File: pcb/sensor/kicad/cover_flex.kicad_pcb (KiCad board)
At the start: 2 copper layers, 32 x 38.7 mm, 7 parts, among them J1 S7081-42R +5V, J2 S7081-42R GND, J3 S7081-42R VBAT, J4 S7081-42R GND, U1 TLV75533PDBVR

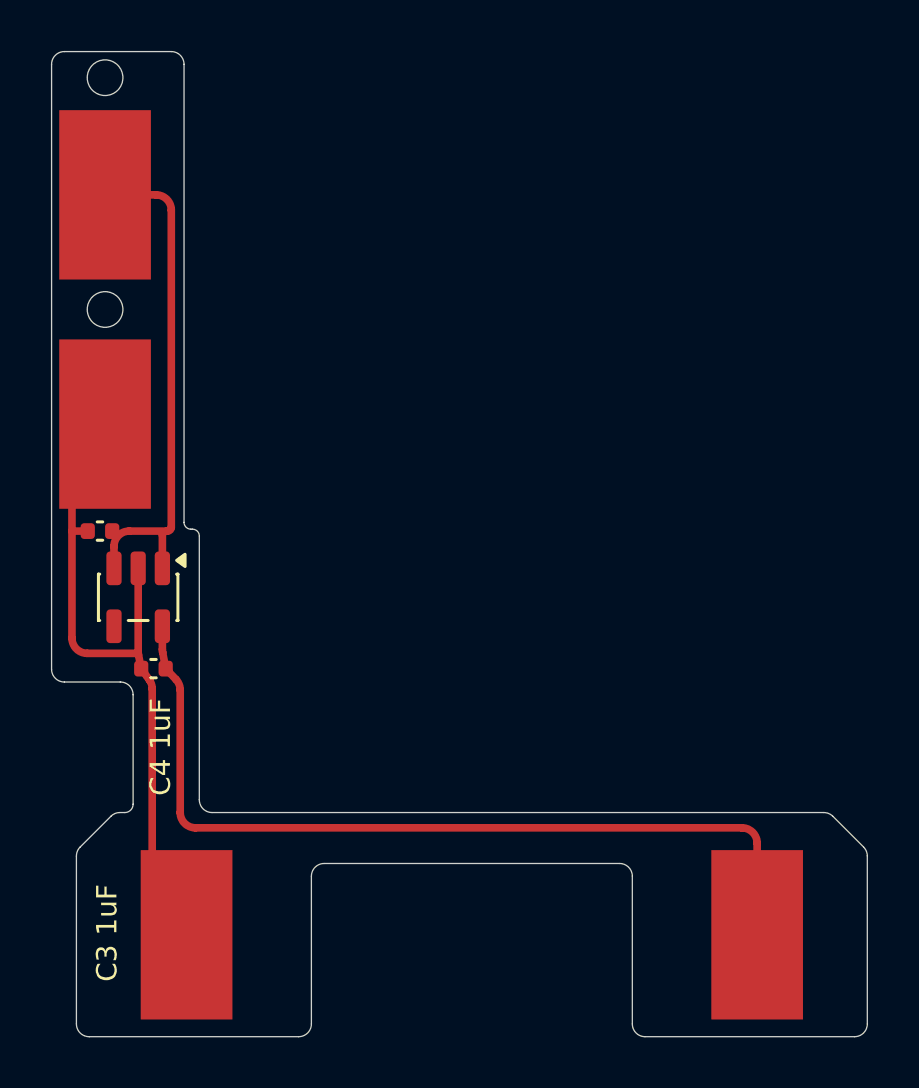
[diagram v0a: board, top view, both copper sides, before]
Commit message: Back cover: snap hooks for the flex, stronger magnet clips, rounded contact posts; #6 countersink and PLATE_Y on the trim
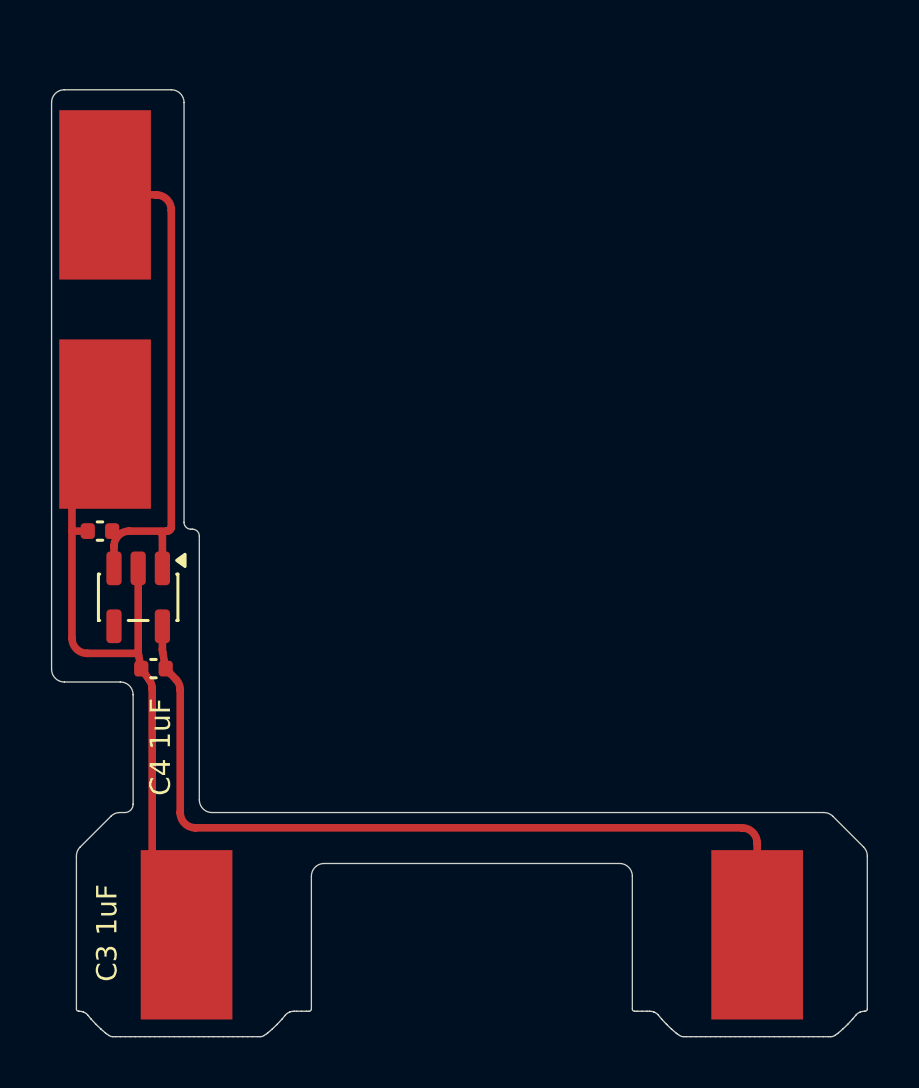
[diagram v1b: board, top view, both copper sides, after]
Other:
- board size 32 x 38.7 mm -> 32 x 37.2 mm
- board text added: "STIFFENER FR4 0.8 mm, back side, flush with the long edges (snap hooks)"
- board text removed: "STIFFENER FR4 0.3 mm, back side, with the peg holes"

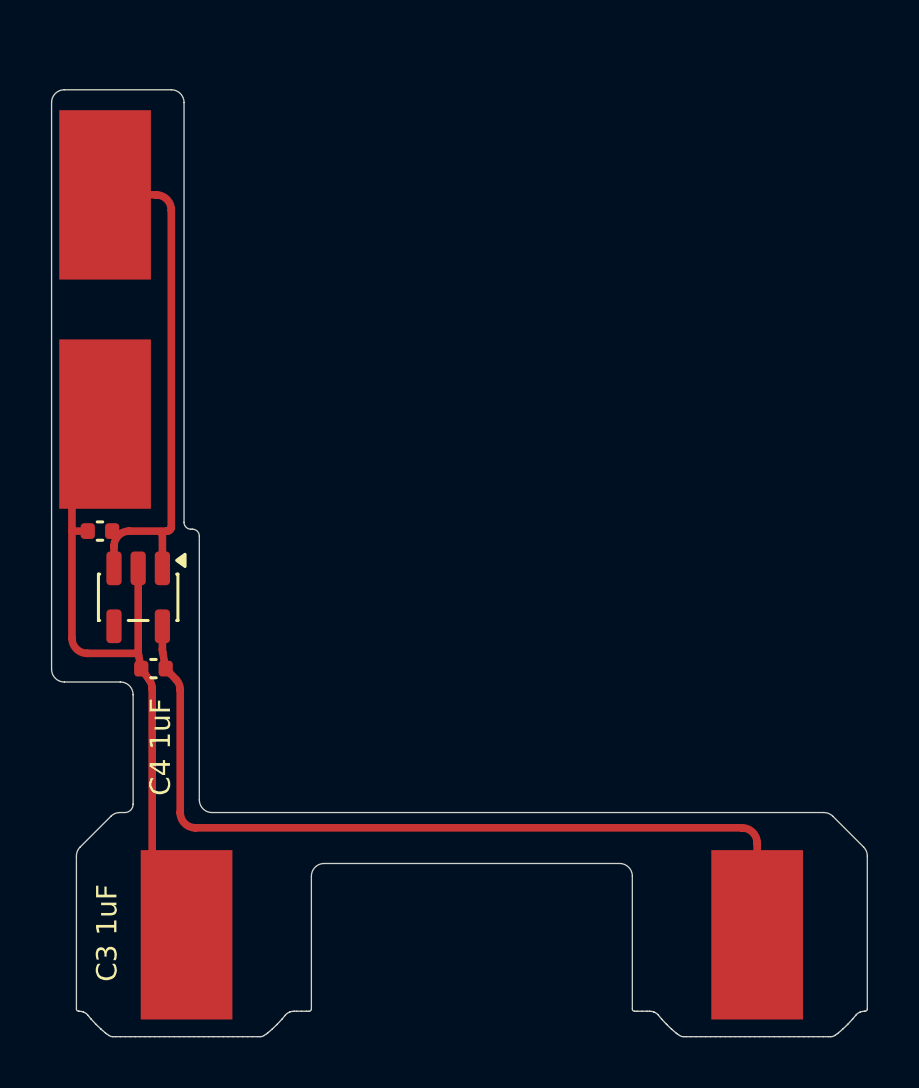
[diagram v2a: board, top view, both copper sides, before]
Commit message: Boards for v0.4: ring board, mic carrier, riser, cover flex, EU cap board, wiring board posts
- Ring board, mic carrier and riser in pcb/sensor/ (D-50, D-60, D-68); carrier and riser fab
  packs; the ring board waits on the MSR-2's CN2 part and map
- Riser 14 x 12 mm, pins above and between the posts; cover flex with the run past the GND
  contact post and a jog from the pad section (D-79)
- EU cap board on the carrier, closed snap windows, wider with the face plate (D-56, D-70,
  D-77, D-78); EU 5 V board pins follow the back cover's pads
- Wiring board: WA-SMSI spacer posts in the 5 V area (SMT, spigot inside the board), J2
- ERC / DRC clean on every board
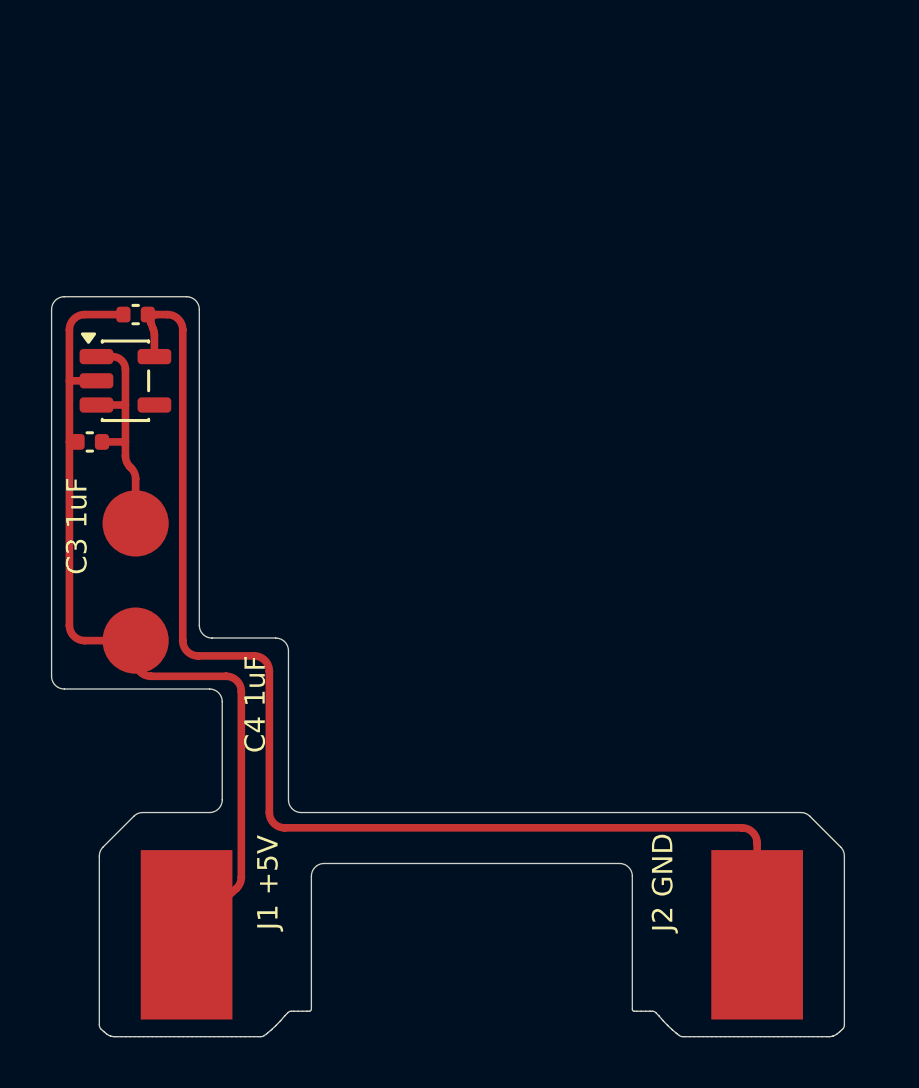
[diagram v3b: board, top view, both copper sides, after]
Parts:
- J1: value S7081-42R +5V -> +5V pin pad; footprint sensor:Harwin_S7081-42R -> sensor:Contact_Pad_D2.6mm
- J2: value S7081-42R GND -> GND pin pad; footprint sensor:Harwin_S7081-42R -> sensor:Contact_Pad_D2.6mm
- moved C4 13.9 mm to (86.8, 100.7)
- moved J1 13.0 mm to (86.8, 108.9), turned to 0 degrees
- moved J2 8.58 mm to (86.8, 113.5), turned to 0 degrees
- moved U1 8.51 mm to (86.4, 103.3), turned to 0 degrees
- moved C3 3.52 mm to (85.0, 105.7)
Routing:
- net +3V3: track 34.4 -> 48.3 mm
- net +5V: track 20.3 -> 9.61 mm
- net GND: track 27.2 -> 34.4 mm
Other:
- board size 32 x 37.2 mm -> 31.1 x 29.1 mm
- board text added: "J1 +5V"
- board text added: "J2 GND"
- board text removed: "J1 S7081-42R"
- board text removed: "J2 S7081-42R"
